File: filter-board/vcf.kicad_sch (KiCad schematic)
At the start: 42 parts, among them U1 TL074, U3 TL074, U4 SSI2164-Split

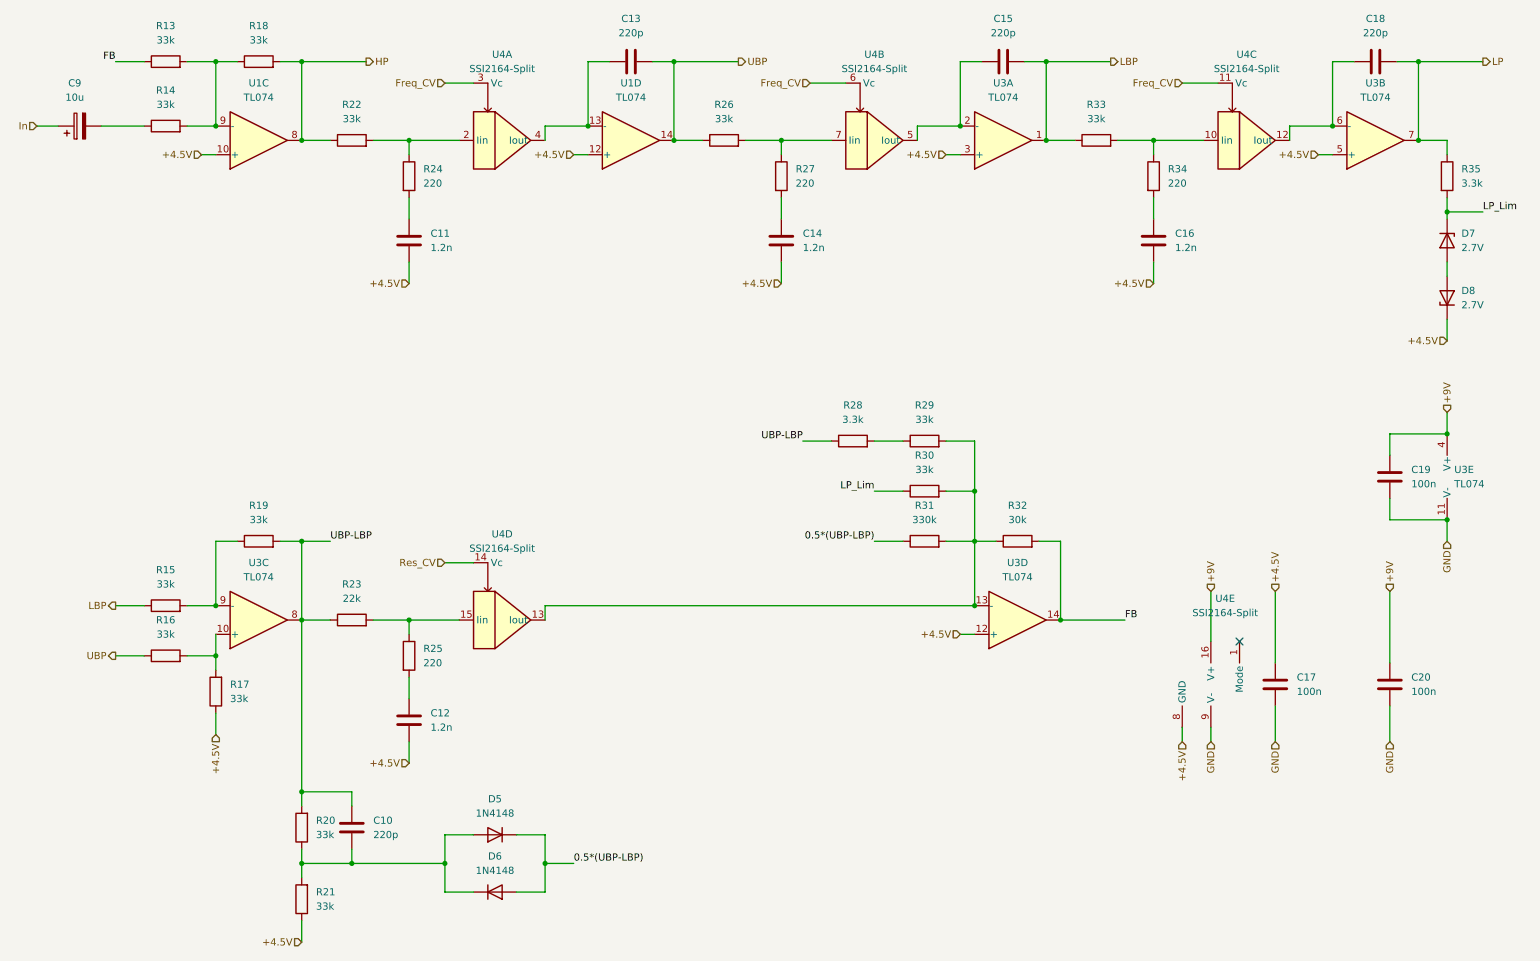
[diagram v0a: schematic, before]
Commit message: Filter board layout
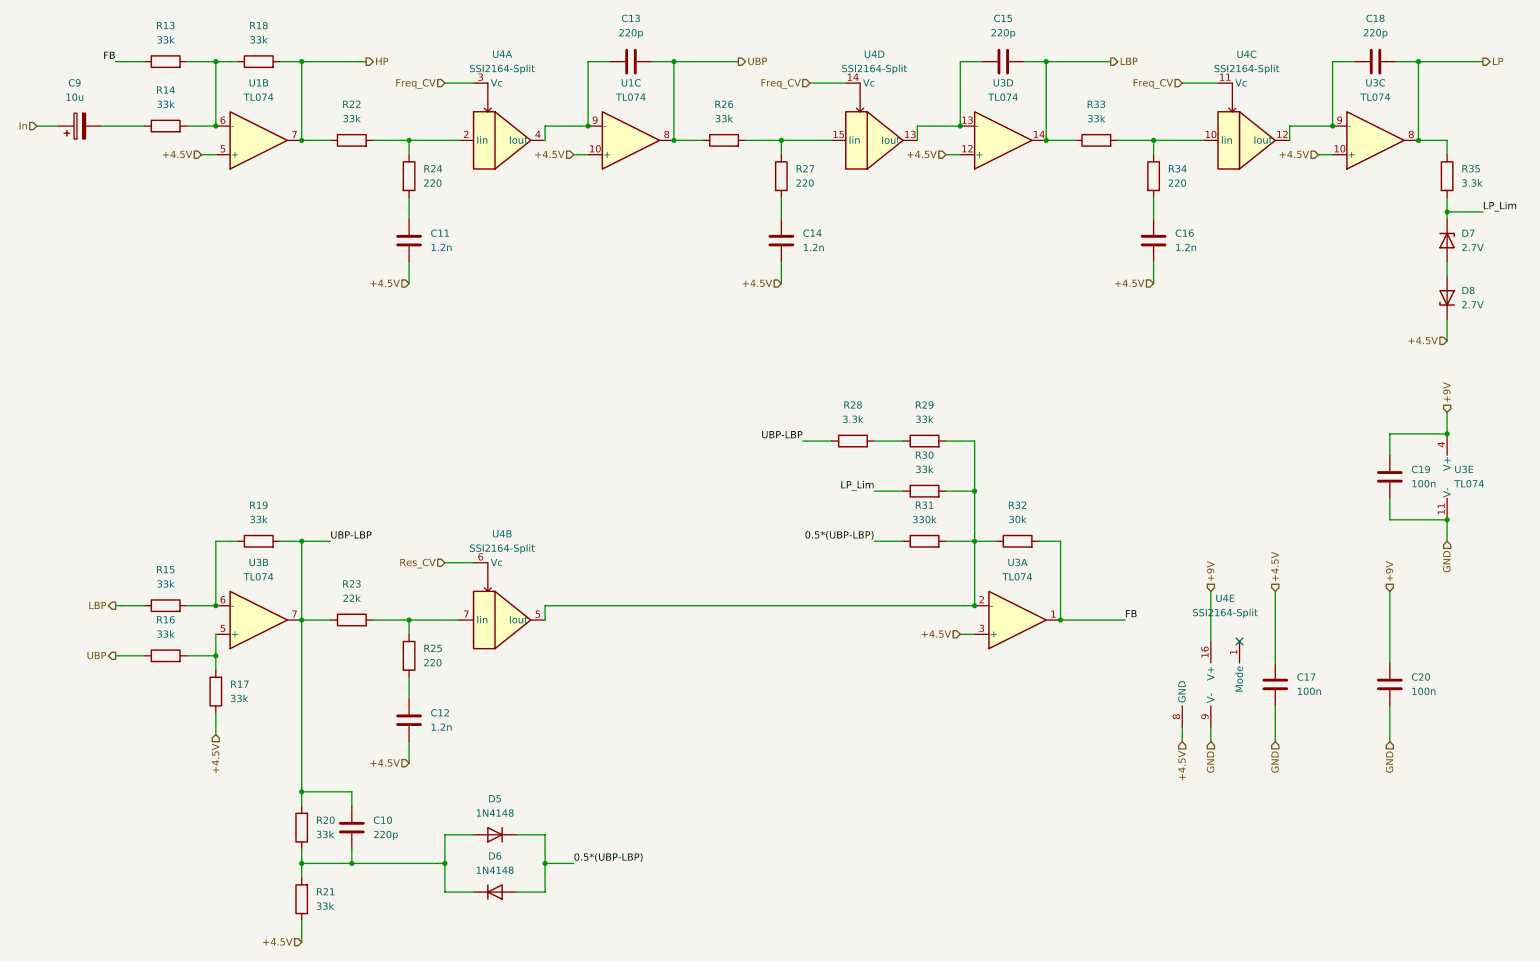
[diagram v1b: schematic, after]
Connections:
- net +4.5V: now also U1.10 (+), U1.5 (+), U3.10 (+), U3.12 (+), U3.3 (+); no longer U1.10 (+), U1.12 (+), U3.12 (+), U3.3 (+), U3.5 (+)
- net FB: now also U3.1; no longer U3.14
- net Freq_CV: now also U4.14 (Vc); no longer U4.6 (Vc)
- net HP: now also U1.7; no longer U1.8
- net LBP: now also U3.14; no longer U3.1
- net LP: now also U3.8; no longer U3.7
- net Res_CV: now also U4.6 (Vc); no longer U4.14 (Vc)
- net UBP: now also U1.8; no longer U1.14
- net UBP-LBP: now also U3.7; no longer U3.8
- net at R13.2, R14.2, R18.1: now also U1.6 (-); no longer U1.9 (-)
- net at C18.1, U4.12 (Iout): now also U3.9 (-); no longer U3.6 (-)
- net at R26.2, R27.1: now also U4.15 (Iin); no longer U4.7 (Iin)
- net at R29.2, R30.2, R31.2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: now also U3.2 (-), U4.5 (Iout); no longer U3.13 (-), U4.13 (Iout)
- net at R16.2, R17.2: now also U3.5 (+); no longer U3.10 (+)
- net at R15.2, R19.1: now also U3.6 (-); no longer U3.9 (-)
- net at R23.2, R25.1: now also U4.7 (Iin); no longer U4.15 (Iin)
- net at C13.1, U4.4 (Iout): now also U1.9 (-); no longer U1.13 (-)
- new net: C15.1, U3.13 (-), U4.13 (Iout)
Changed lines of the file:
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@@
     (pin "2")
   )
-  (symbol (lib_id "pedals:SSI2164-Split") (at 167.64 52.07 0) (unit 2)
+  (symbol (lib_id "pedals:SSI2164-Split") (at 167.64 52.07 0) (unit 4)
     (in_bom yes) (on_board yes) (fields_autoplaced)
     (property "Reference" "U4" (id 0) (at 167.64 36.83 0))
@@
     (pin "2")
   )
-  (symbol (lib_id "Amplifier_Operational:TL074") (at 58.42 137.16 0) (mirror x) (unit 3)
+  (symbol (lib_id "Amplifier_Operational:TL074") (at 58.42 137.16 0) (mirror x) (unit 2)
     (in_bom yes) (on_board yes) (fields_autoplaced)
     (property "Reference" "U3" (id 0) (at 58.42 127 0))
@@
     (pin "9")
   )
-  (symbol (lib_id "Amplifier_Operational:TL074") (at 256.54 52.07 0) (mirror x) (unit 2)
+  (symbol (lib_id "Amplifier_Operational:TL074") (at 256.54 52.07 0) (mirror x) (unit 3)
     (in_bom yes) (on_board yes) (fields_autoplaced)
     (property "Reference" "U3" (id 0) (at 256.54 41.91 0))
@@
     (pin "2")
   )
-  (symbol (lib_id "pedals:SSI2164-Split") (at 101.6 137.16 0) (unit 4)
+  (symbol (lib_id "pedals:SSI2164-Split") (at 101.6 137.16 0) (unit 2)
     (in_bom yes) (on_board yes) (fields_autoplaced)
     (property "Reference" "U4" (id 0) (at 101.6 121.92 0))
@@
     (pin "2")
   )
-  (symbol (lib_id "Amplifier_Operational:TL074") (at 193.04 137.16 0) (mirror x) (unit 4)
+  (symbol (lib_id "Amplifier_Operational:TL074") (at 193.04 137.16 0) (mirror x) (unit 1)
     (in_bom yes) (on_board yes) (fields_autoplaced)
     (property "Reference" "U3" (id 0) (at 193.04 127 0))
@@
     (pin "4")
   )
-  (symbol (lib_id "Amplifier_Operational:TL074") (at 124.46 52.07 0) (mirror x) (unit 4)
+  (symbol (lib_id "Amplifier_Operational:TL074") (at 124.46 52.07 0) (mirror x) (unit 3)
     (in_bom yes) (on_board yes) (fields_autoplaced)
     (property "Reference" "U1" (id 0) (at 124.46 41.91 0))
@@
     (pin "2")
   )
-  (symbol (lib_id "Amplifier_Operational:TL074") (at 58.42 52.07 0) (mirror x) (unit 3)
+  (symbol (lib_id "Amplifier_Operational:TL074") (at 58.42 52.07 0) (mirror x) (unit 2)
     (in_bom yes) (on_board yes) (fields_autoplaced)
     (property "Reference" "U1" (id 0) (at 58.42 41.91 0))
@@
     (pin "2")
   )
-  (symbol (lib_id "Amplifier_Operational:TL074") (at 190.5 52.07 0) (mirror x) (unit 1)
+  (symbol (lib_id "Amplifier_Operational:TL074") (at 190.5 52.07 0) (mirror x) (unit 4)
     (in_bom yes) (on_board yes) (fields_autoplaced)
     (property "Reference" "U3" (id 0) (at 190.5 41.91 0))

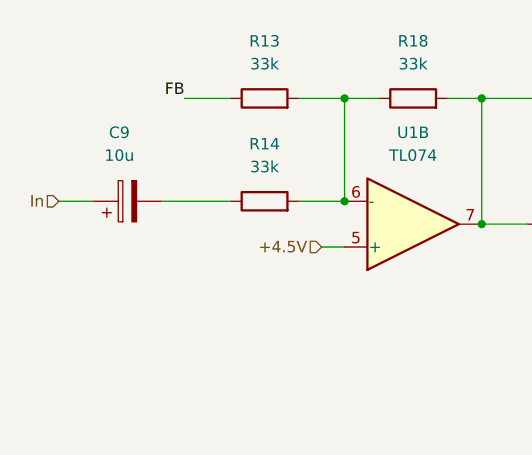
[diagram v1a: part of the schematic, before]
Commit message: Follower schem done
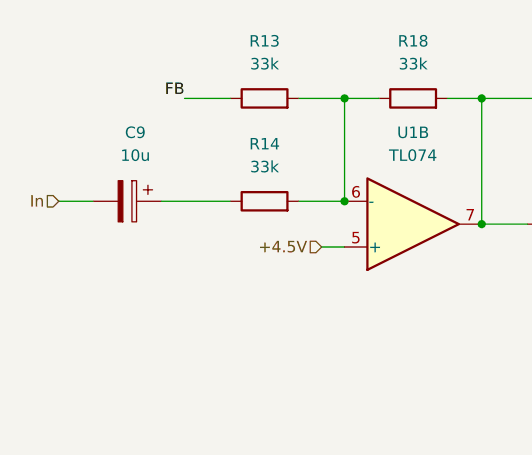
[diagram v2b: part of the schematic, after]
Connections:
- net In: now also C9.2; no longer C9.1
- net at R14.1: now also C9.1; no longer C9.2
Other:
- moved on the sheet: C9
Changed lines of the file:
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@@
     (pin "4")
   )
-  (symbol (lib_id "Device:C_Polarized") (at 26.67 49.53 90) (unit 1)
+  (symbol (lib_id "Device:C_Polarized") (at 26.67 49.53 270) (unit 1)
     (in_bom yes) (on_board yes) (fields_autoplaced)
-    (property "Reference" "C9" (id 0) (at 25.781 41.91 90))
-    (property "Value" "10u" (id 1) (at 25.781 44.45 90))
-    (property "Footprint" "Capacitor_SMD:CP_Elec_5x5.4" (id 2) (at 30.48 48.5648 0)
+    (property "Reference" "C9" (id 0) (at 27.559 41.91 90))
+    (property "Value" "10u" (id 1) (at 27.559 44.45 90))
+    (property "Footprint" "Capacitor_SMD:CP_Elec_5x5.4" (id 2) (at 22.86 50.4952 0)
       (effects (font (size 1.27 1.27)) hide)
     )
